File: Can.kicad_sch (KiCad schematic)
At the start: 16 parts, among them U65 TD541SCANH

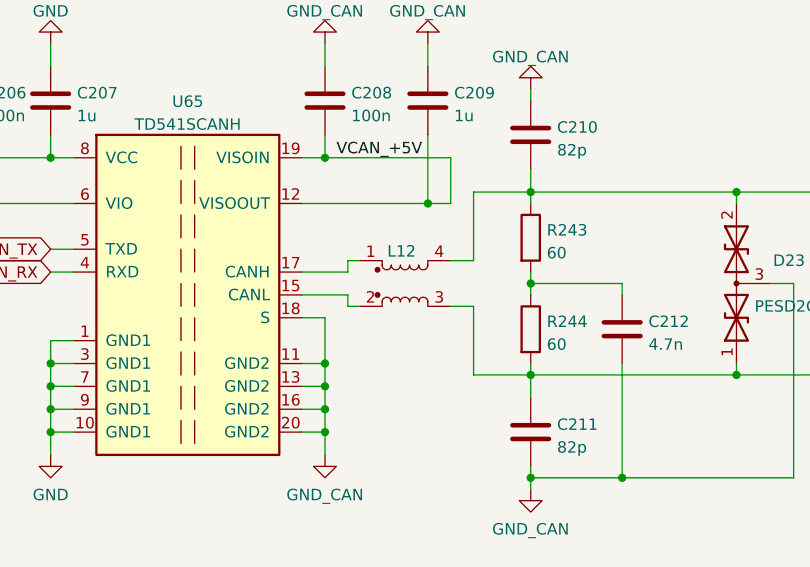
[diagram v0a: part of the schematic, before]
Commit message: Изменения в схеме: убрал разъемы датчиков тока
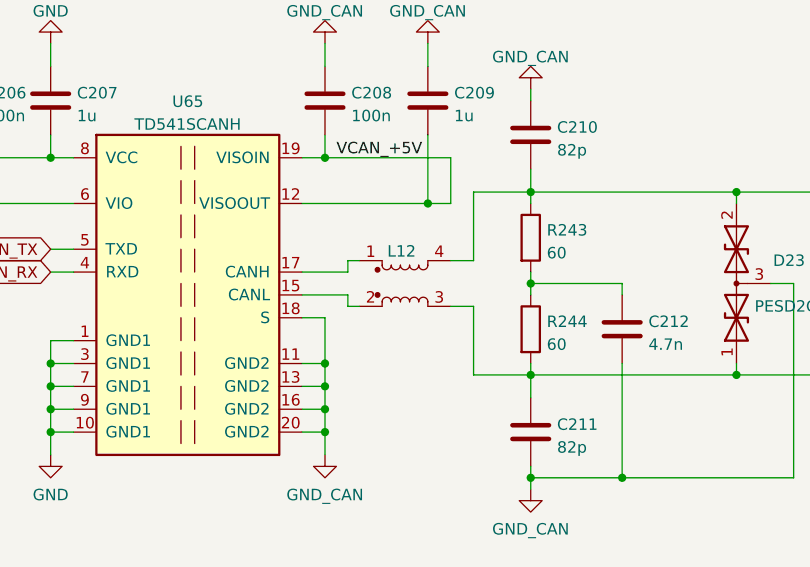
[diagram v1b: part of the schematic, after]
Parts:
- L12: value DR331-513AE -> DR331-513AE

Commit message: Изменения: развел все
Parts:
- R284: value 1.5k -> 1k
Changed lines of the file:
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@@
 		(fields_autoplaced yes)
 		(property "Reference" "R284"
-			(at 179.578 56.3153 0)
+			(at 180.34 55.8799 0)
 			(effects
 				(font
@@
 			)
 		)
-		(property "Value" "1.5k"
-			(at 179.578 58.8522 0)
+		(property "Value" "1k"
+			(at 180.34 58.4199 0)
 			(effects
 				(font

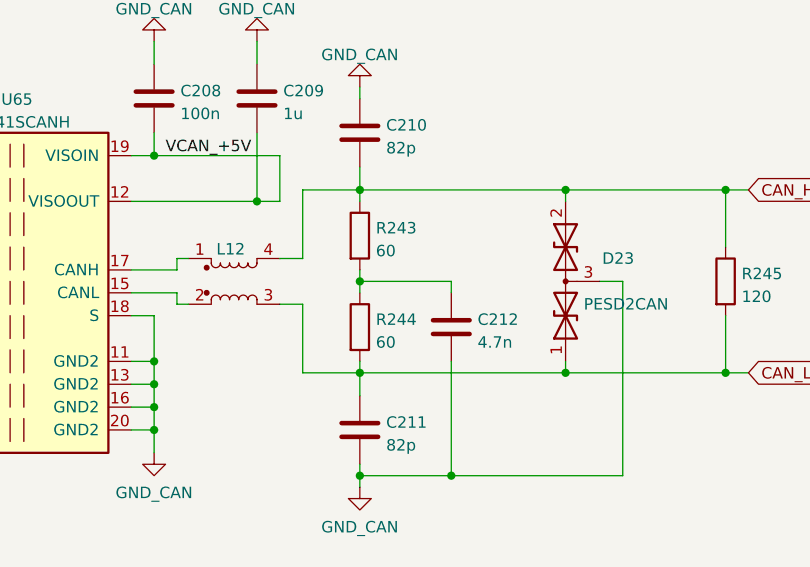
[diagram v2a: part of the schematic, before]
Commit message: Изменения: испарвил номиналы на схеме в соответствии с BOM
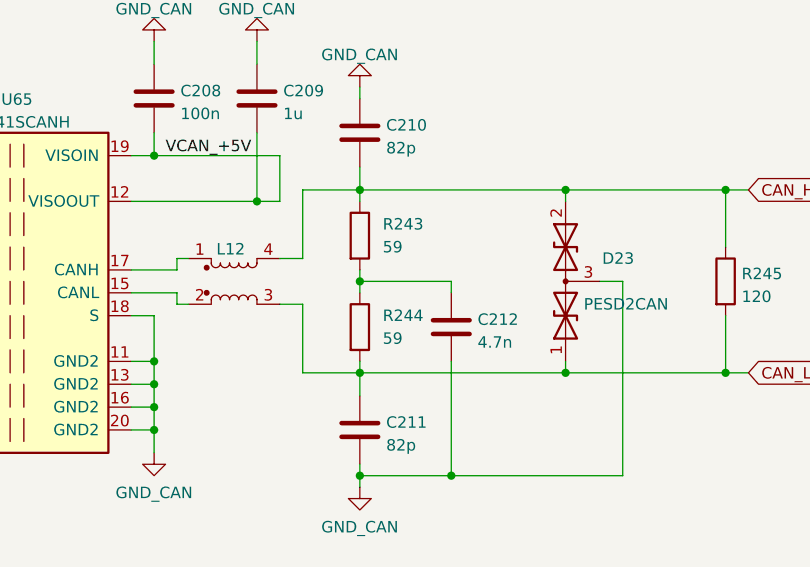
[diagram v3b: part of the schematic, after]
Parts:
- R243, R244: value 60 -> 59
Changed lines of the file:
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@@
 		(fields_autoplaced yes)
 		(property "Reference" "R244"
-			(at 163.068 105.8453 0)
-			(effects
-				(font
-					(size 1.27 1.27)
-				)
-				(justify left)
-			)
-		)
-		(property "Value" "60"
-			(at 163.068 108.3822 0)
+			(at 163.83 105.4099 0)
+			(effects
+				(font
+					(size 1.27 1.27)
+				)
+				(justify left)
+			)
+		)
+		(property "Value" "59"
+			(at 163.83 107.9499 0)
 			(effects
 				(font
@@
 		(fields_autoplaced yes)
 		(property "Reference" "R243"
-			(at 163.068 95.6853 0)
-			(effects
-				(font
-					(size 1.27 1.27)
-				)
-				(justify left)
-			)
-		)
-		(property "Value" "60"
-			(at 163.068 98.2222 0)
-			(effects
-				(font
+			(at 163.83 95.2499 0)
+			(effects
+				(font
+					(size 1.27 1.27)
+				)
+				(justify left)
+			)
+		)
+		(property "Value" "59"
+			(at 163.83 97.7899 0)
+			(effects
+				(font

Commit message: REV_C: добавил Э3
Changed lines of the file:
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@@
 (kicad_sch
-	(version 20231120)
+	(version 20250114)
 	(generator "eeschema")
-	(generator_version "8.0")
+	(generator_version "9.0")
 	(paper "A4")
+	(title_block
+		(comment 1 "НВЦТ.EVP150-2-1.3000.100 Э3")
+	)
 	(junction
 		(at 161.29 91.44)
@@
 	(label "VCAN_+5V"
 		(at 177.8 48.26 180)
-		(fields_autoplaced yes)
 		(effects
 			(font
@@
 	(label "VCAN_+5V"
 		(at 139.7 87.63 0)
-		(fields_autoplaced yes)
 		(effects
 			(font
